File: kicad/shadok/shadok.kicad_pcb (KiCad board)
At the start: 2 copper layers, 134.6 x 76.5 mm, 158 parts, among them J101 Conn_01x07_Female, J102 GS3, J103 TEST_1P, J104 TEST_1P, J105 SERIALS, J401 Conn_02x05_Odd_Even, J501 Micro_SD_Card, J502 TEST_1P, J601 74LVC8T245, J602 74LVC8T245, J603 74LVC8T245, J604 SNP34-90, J605 74LVC8T245, J701 DB9_Male_MountingHoles, J702 DB9_Male_MountingHoles, J801 Conn_01x02, J815 Audio Out, J901 Conn_02x04_Odd_Even, J913 DIN-5, Q901 BC817, Q902 BC807, Q903 BC817, SW101 SW_Push, U201 ADP2108-1.2, U202 LP2985-2.5, U203 ADP2108-3.3, U301 IS42S16400J, U401 EPCS4SI8N, U501 ESP12F, U601 74LVC1T45, U701 MCP23S17, U801 TPA6110A2, X101 KXO-V97 50MHz

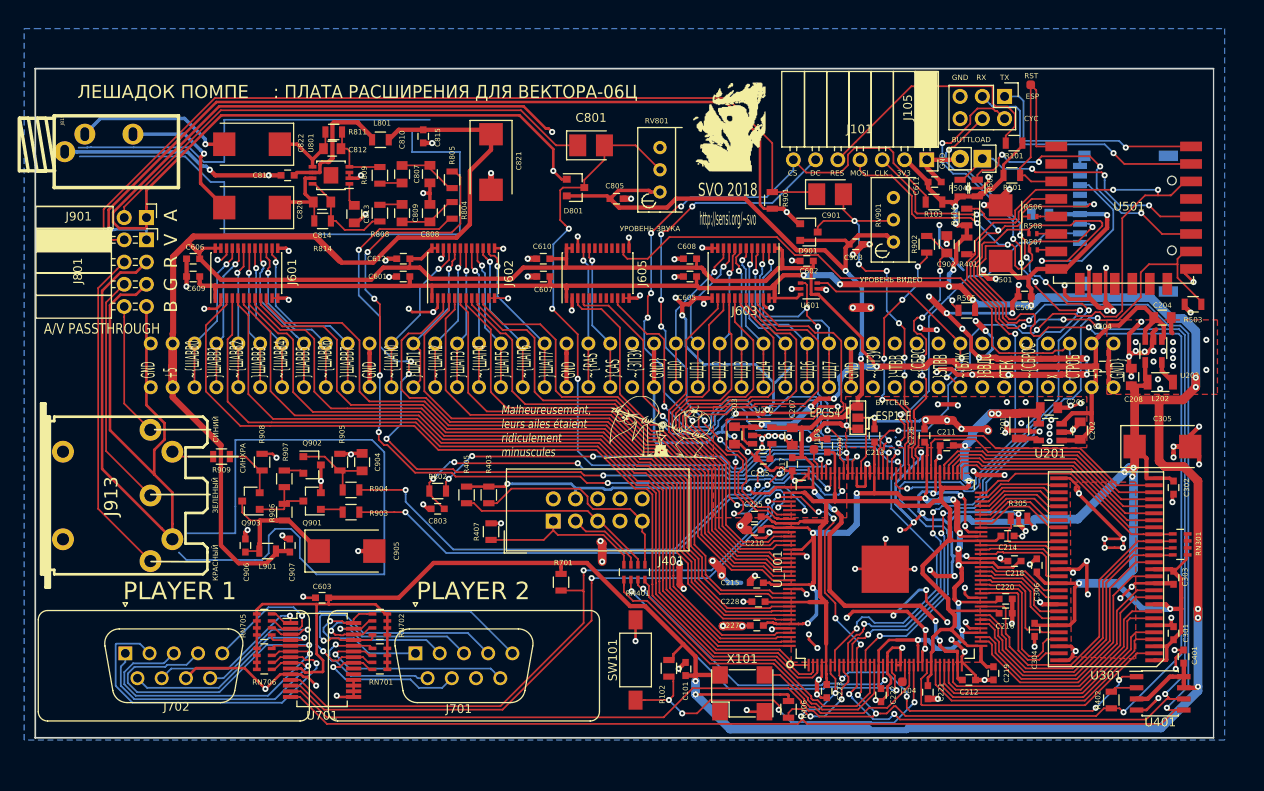
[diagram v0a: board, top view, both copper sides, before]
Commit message: fixed the fuckups from the first version
had to remove video module
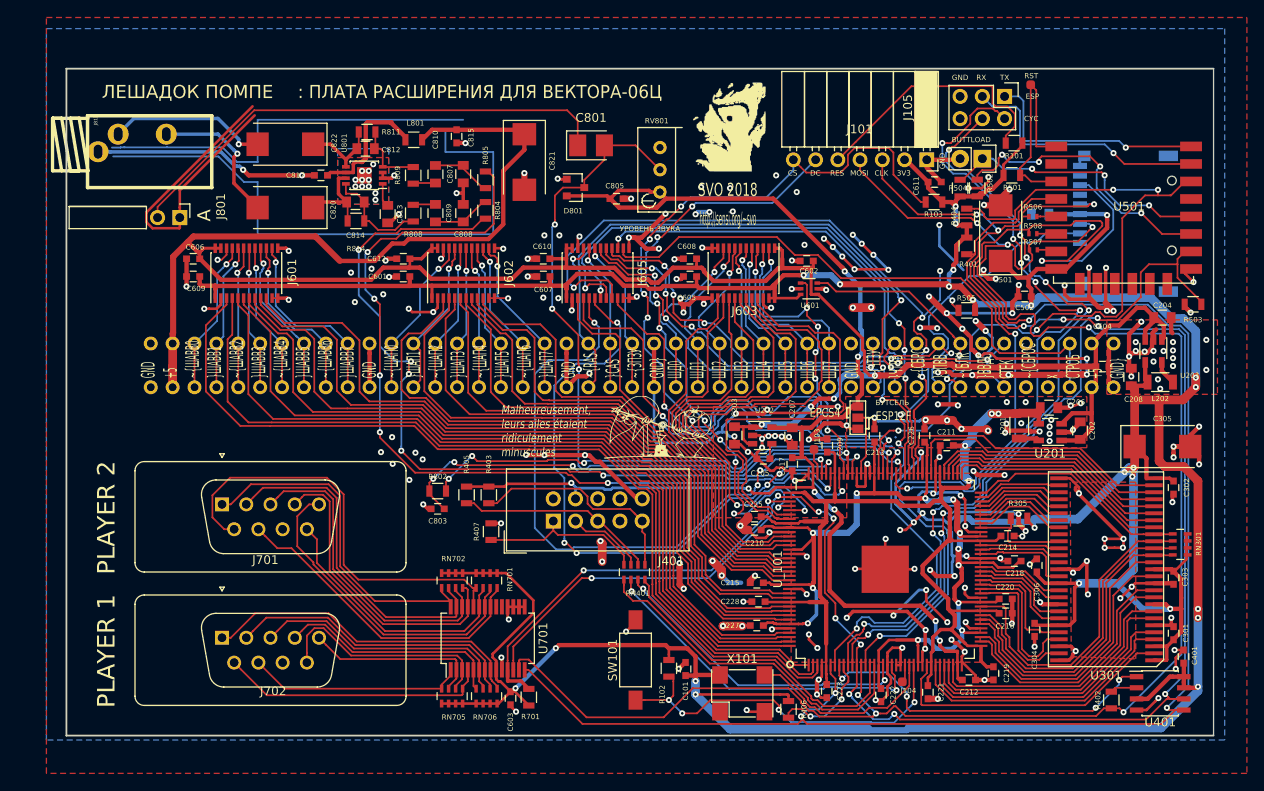
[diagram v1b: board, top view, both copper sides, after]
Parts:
- removed C901: 10.0, Capacitors_Tantalum_SMD:CP_Tantalum_Case-B_EIA-3528-21_Reflow
- removed C902: 220, Capacitors_SMD:C_0805
- removed C903, C906, C907: 0.1, Capacitors_SMD:C_0603
- removed C904: 33, Capacitors_SMD:C_0805
- removed C905: 68.0, Capacitors_Tantalum_SMD:CP_Tantalum_Case-D_EIA-7343-31_Reflow
- removed D901: BAT54S, TO_SOT_Packages_SMD:SOT-23
- removed J901: Conn_02x04_Odd_Even, Socket_Strips:Socket_Strip_Angled_2x04_Pitch2.54mm
- removed J913: DIN-5, w_conn_av:din-5
- removed L901: LQH66SN101M 100uH, Resistors_SMD:R_0805
- removed Q901, Q903: BC817, TO_SOT_Packages_SMD:SOT-23
- removed Q902: BC807, TO_SOT_Packages_SMD:SOT-23
- removed R901, R909: 75, Resistors_SMD:R_0805
- removed R902: 220, Resistors_SMD:R_0805
- removed R903, R907: 1K2, Resistors_SMD:R_0805
- removed R904: 470, Resistors_SMD:R_0805
- removed R905, R908: 1K, Resistors_SMD:R_0805
- removed R906: 6K8, Resistors_SMD:R_0805
- removed RV901: 100K, Potentiometers:Potentiometer_Bourns_3296W_3-8Zoll_Inline_ScrewUp
- moved J701 27.9 mm to (64.5, 168.7)
- moved RN706 25.8 mm to (94.7, 190.6), turned to 90 degrees
- moved C603 24.4 mm to (97.5, 190.8), turned to 270 degrees
- moved RN705 23.0 mm to (90.8, 190.6), turned to 90 degrees
- moved U701 19.1 mm to (94.9, 184.0), turned to 90 degrees
- moved RN701 15.1 mm to (94.7, 177.4), turned to 270 degrees
- moved R701 13.6 mm to (99.6, 190.7), turned to 270 degrees
- moved J702 11.2 mm to (64.5, 183.9)
- moved RN702 9.66 mm to (90.8, 177.4), turned to 270 degrees
- moved C807 3.81 mm to (92.1, 130.9)
- moved C808 3.81 mm to (92.1, 135.4)
- moved C809 3.81 mm to (88.9, 135.4)
- moved C810 3.81 mm to (88.9, 130.9)
- moved C812 3.81 mm to (80.9, 128.0)
- moved C814 3.81 mm to (79.8, 134.1)
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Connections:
- J604 pad 23: Net-(J604-Pad23) -> /BUS/~ЗПЗУЪ
- J604 pad 34: Net-(J604-Pad34) -> /BUS/~ЧТЗУЪ
- J604 pad 35: Net-(J604-Pad35) -> /BUS/~ЧТВВЪ
- J604 pad 37: Net-(J604-Pad37) -> /BUS/~ЗПВВЪ
- J604 pad 40: Net-(J604-Pad40) -> /BUS/СТЕКЪ
- J605 pad 15: Net-(J605-Pad15) -> /BUS/СТЕКЪ
- J605 pad 16: Net-(J605-Pad16) -> /BUS/~ЗПВВЪ
- J605 pad 17: Net-(J605-Pad17) -> /BUS/~ЧТВВЪ
- J605 pad 18: Net-(J605-Pad18) -> /BUS/~ЧТЗУЪ
- J605 pad 19: Net-(J605-Pad19) -> /BUS/~ЗПЗУЪ
- J605 pad 5: Net-(J605-Pad5) -> /VIDEOBW
- J605 pad 6: Net-(J605-Pad6) -> /HVSYNC
- J605 pad 7: Net-(J605-Pad7) -> /ADC_SYNCp
- J605 pad 8: Net-(J605-Pad8) -> /ADC_SYNCINT
- J605 pad 9: Net-(J605-Pad9) -> /ADC_SYNCn
- U801 pad 9: (no net) -> /anal/POWERPAD
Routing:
- net GND: track 947.2 -> 653.1 mm, vias 218 -> 241
- net /videopass/V06C_CVBS: track 99.9 -> 0.00 mm
- net (no net): track 191.5 -> 113.6 mm
- net /BUS/СТЕКЪ: track 0.00 -> 61.1 mm, vias 0 -> 3
- net /BUS/~ЗПВВЪ: track 0.00 -> 54.6 mm, vias 0 -> 5
- net /ADC_SYNCn: track 33.0 -> 85.0 mm, vias 4 -> 5
- net /BUS/~ЧТВВЪ: track 0.00 -> 47.6 mm, vias 0 -> 4
- net /BUS/~ЧТЗУЪ: track 0.00 -> 46.5 mm, vias 0 -> 4
- net /ADC_SYNCINT: track 30.5 -> 74.3 mm
- net /videopass/PASS_R: track 37.9 -> 0.00 mm
- net /Joysticks/~P2B1: track 18.4 -> 48.7 mm, vias 1 -> 0
- net +3V3: track 664.1 -> 634.2 mm, vias 34 -> 36
- net /DCLK/SPICLK: track 254.8 -> 225.0 mm
- net /~JOY_SS: track 74.9 -> 46.7 mm
- net /videopass/PASS_G: track 27.1 -> 0.00 mm
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- added copper zone on B.Cu, net /anal/POWERPAD
- added copper zone on F.Cu, net /anal/POWERPAD
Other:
- board size 134.6 x 76.5 mm -> 131.1 x 76.2 mm
- board text removed: "A/V PASSTHROUGH"
- board text removed: "B"
- board text removed: "G"
- board text removed: "R"
- board text removed: "V"
- board text removed: "ЗЕЛЕНЫЙ"
- board text removed: "КРАСНЫЙ"
- board text removed: "СИНИЙ"
- board text removed: "СИНХРА"
- board text removed: "УРОВЕНЬ ВИДЕО"
